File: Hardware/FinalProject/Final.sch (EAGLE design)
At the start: 47 parts, among them IC1 LM2937

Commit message: Changed to SMD caps near TM4C
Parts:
- removed C10: 2.2uf, EE445L:CAPACITOR025-024X044
- removed C7, C8, C9: 0.1uf, EE445L:CAPACITOR025-024X044
- added C21: 4.7uF, EE445L:CAPACITORC0603K
- added UART: (no value), EE445L:PINHD-1X5
- C1, C3: value 0.01uf -> 4.7uF; device EE445L:CAPACITOR025-024X044 -> EE445L:CAPACITORC0603K
- C2: value 0.1uf -> 4.7uF; device EE445L:CAPACITOR025-024X044 -> EE445L:CAPACITORC0603K
- C4: value 0.1uf -> 2.2uF; device EE445L:CAPACITOR025-024X044 -> EE445L:CAPACITORC0603K
- C5: value 0.01uf -> 1uF; device EE445L:CAPACITOR025-024X044 -> EE445L:CAPACITORC0603K
- C6: value 1.0uf -> 0.1uF; device EE445L:CAPACITOR025-024X044 -> EE445L:CAPACITORC0603K
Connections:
- removed net PA0: U$1G$1.PA0
- removed net PB4: U$1G$2.PB4
- new net N$5: UART.5
- new net URX: U$1G$1.PA0, UART.3
- new net UTX: U$1G$1.PA1, UART.2
- net +3V3: now also C21.1, UART.1; no longer C4.1, C5.1, C6.1
- net GND: now also C21.2, UART.4; no longer C10.2, C7.2, C8.2, C9.2
- net ST7735_TFT_CS_2: now also U$1G$2.PB4; no longer U$1G$1.PA1
- net VDDC: now also C4.1, C5.1, C6.1; no longer C10.1, C7.1, C8.1, C9.1
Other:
- moved on the sheet: C1, C2, C4, C5, C6

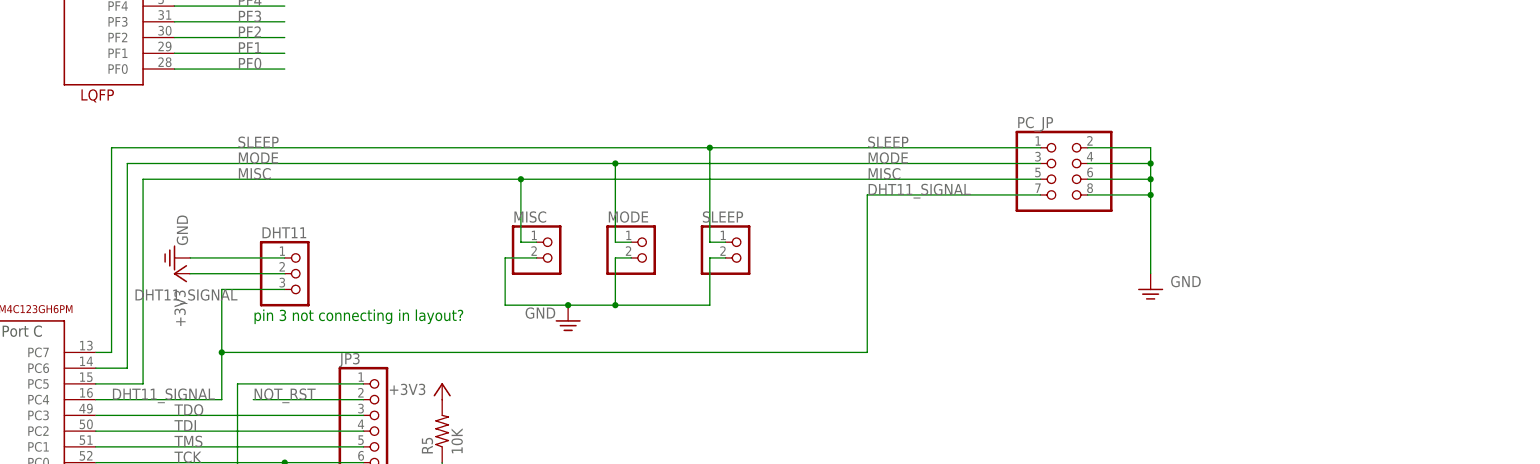
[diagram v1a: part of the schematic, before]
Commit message: Add lib and fixed cap placement
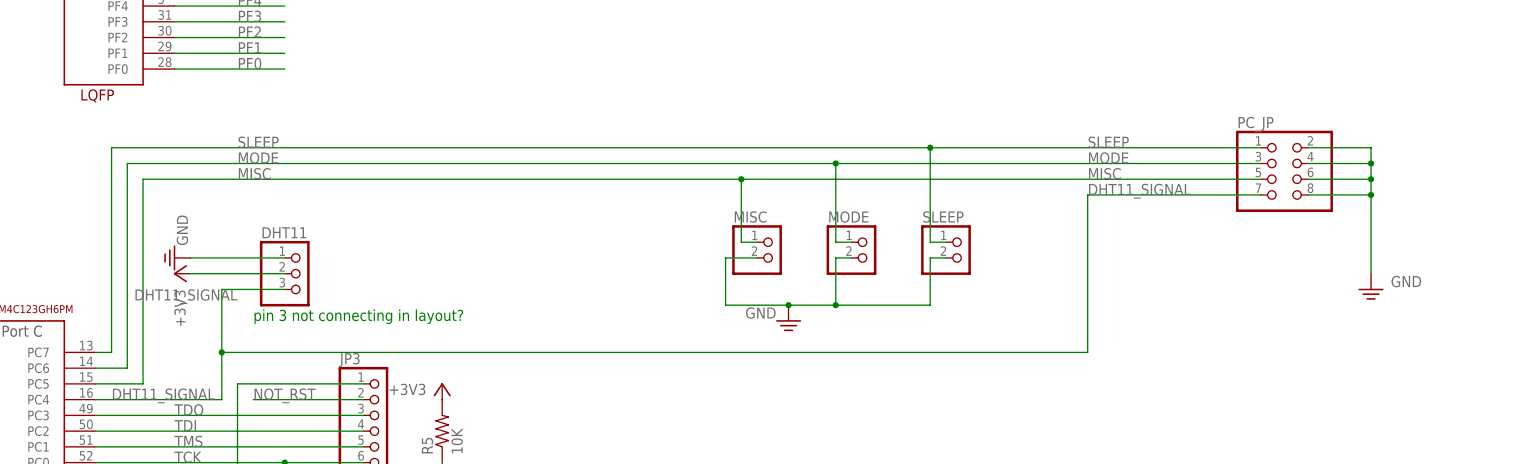
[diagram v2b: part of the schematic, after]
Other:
- moved on the sheet: MISC, MODE, PC_JP, SLEEP
